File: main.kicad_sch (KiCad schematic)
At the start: 80 parts, among them SW1 Kailh-Choc, SW10 Kailh-Choc, SW11 Kailh-Choc, SW12 Kailh-Choc, SW13 Kailh-Choc, SW14 Kailh-Choc, SW15 Kailh-Choc, SW16 Kailh-Choc, SW17 Kailh-Choc, SW18 Kailh-Choc, SW19 Kailh-Choc, SW2 Kailh-Choc, SW20 Kailh-Choc, SW21 Kailh-Choc, SW22 Kailh-Choc, SW23 Kailh-Choc, SW24 Kailh-Choc, SW25 Kailh-Choc, SW26 Kailh-Choc, SW27 Kailh-Choc, SW28 Kailh-Choc, SW29 Kailh-Choc, SW3 Kailh-Choc, SW30 Kailh-Choc, SW31 Kailh-Choc, SW32 Kailh-Choc, SW33 Kailh-Choc, SW34 Kailh-Choc, SW4 Kailh-Choc, SW5 Kailh-Choc, SW6 Kailh-Choc, SW7 Kailh-Choc, SW8 Kailh-Choc, SW9 Kailh-Choc, U1 nice_nano, U2 nice_nano

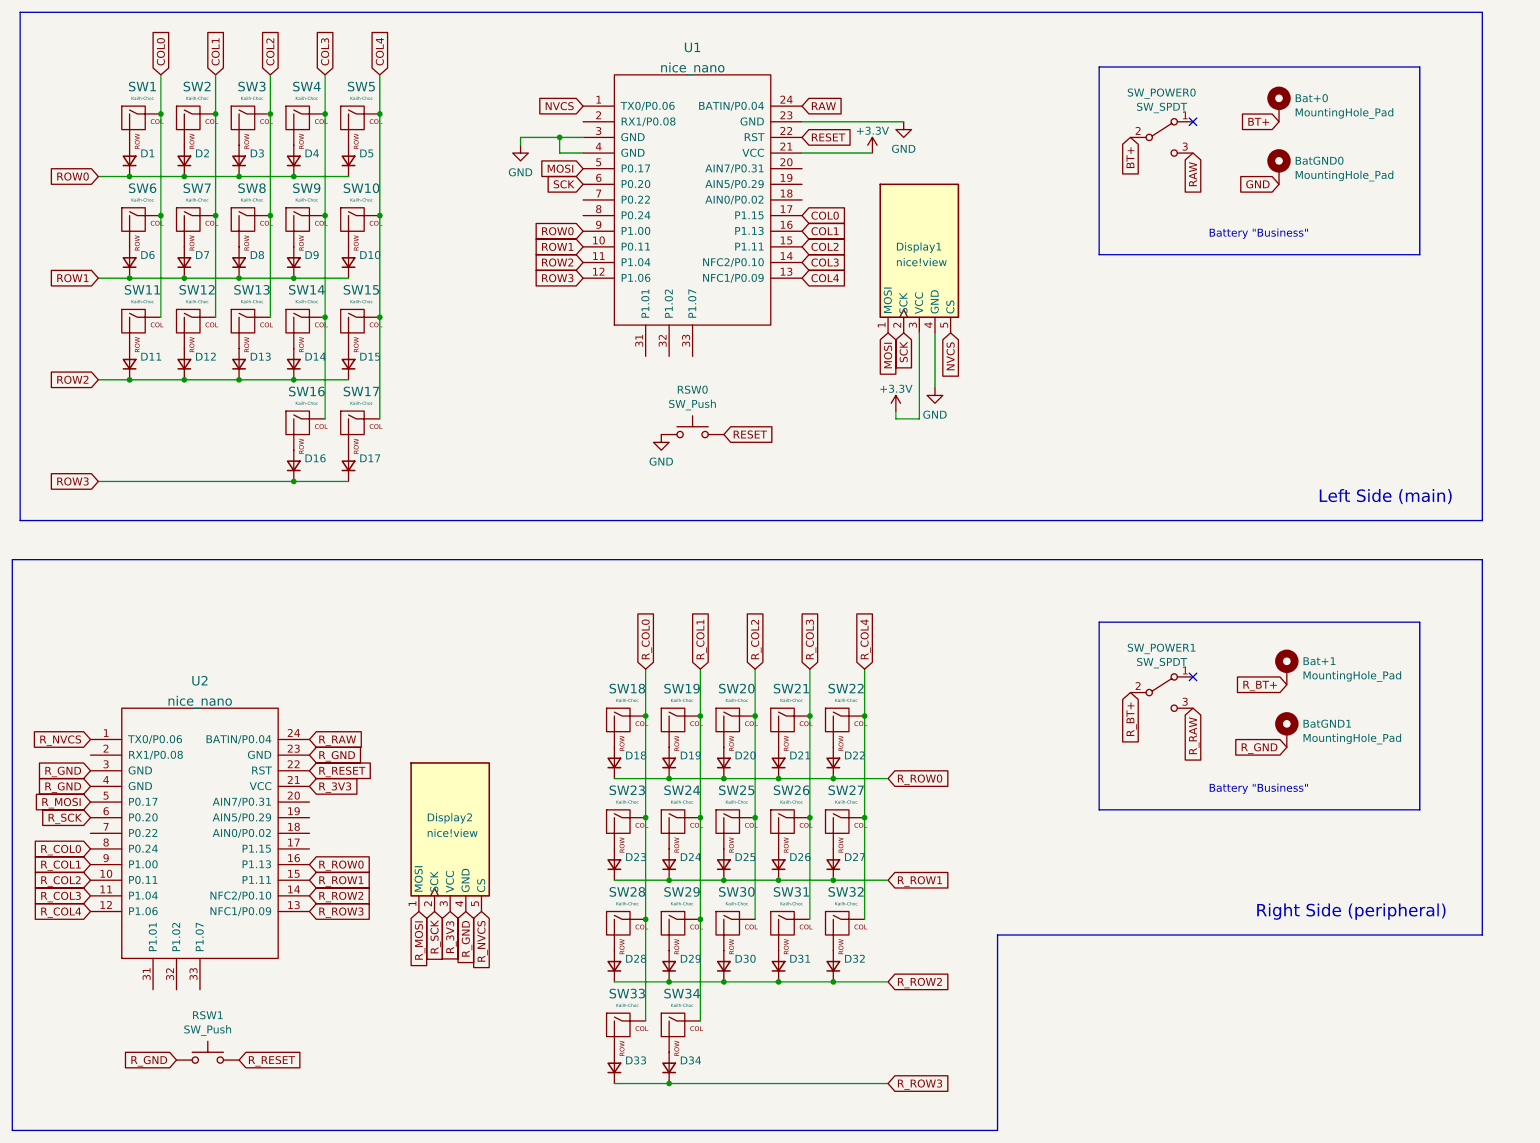
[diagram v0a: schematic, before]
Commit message: Added missing parts to schematic.
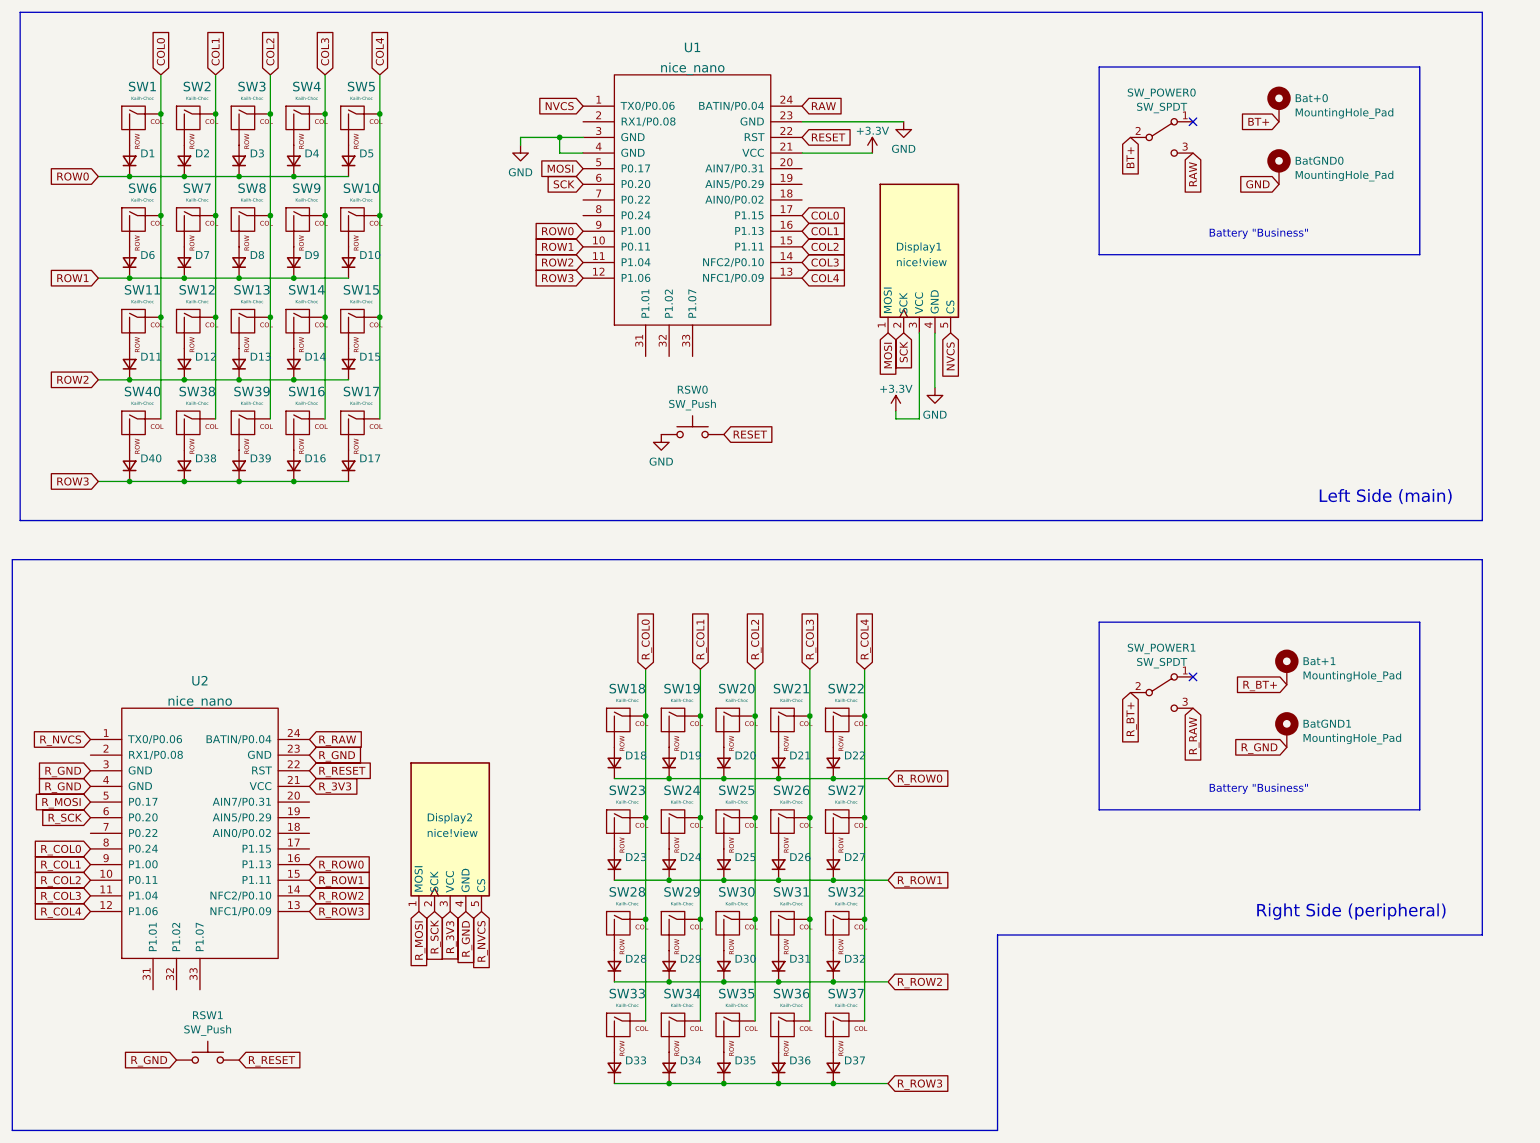
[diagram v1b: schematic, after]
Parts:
- added D35, D36, D37, D38, D39, D40: diode, urchin-footprints:SMD_Diode_Tiny, symbol Device:D_Small
- added SW35, SW36, SW37, SW38, SW39, SW40: Kailh-Choc, urchin-footprints:SW_Hotswap_Kailh_Choc_V1_tweaked, symbol MX_Alps_Hybrid:MX-NoLED
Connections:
- net COL0: now also SW40.1 (COL)
- net COL1: now also SW38.1 (COL)
- net COL2: now also SW39.1 (COL)
- net ROW3: now also D38.1 (K), D39.1 (K), D40.1 (K)
- net R_COL2: now also SW35.1 (COL)
- net R_COL3: now also SW36.1 (COL)
- net R_COL4: now also SW37.1 (COL)
- net R_ROW3: now also D35.1 (K), D36.1 (K), D37.1 (K)
- new net: D35.2 (A), SW35.2 (ROW)
- new net: D37.2 (A), SW37.2 (ROW)
- new net: D36.2 (A), SW36.2 (ROW)
- new net: D39.2 (A), SW39.2 (ROW)
- new net: D40.2 (A), SW40.2 (ROW)
- new net: D38.2 (A), SW38.2 (ROW)

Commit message: Updated schematic and updated pcb
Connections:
- net COL0: now also SW38.1 (COL); no longer SW40.1 (COL)
- net COL1: now also SW39.1 (COL); no longer SW38.1 (COL)
- net COL2: now also SW40.1 (COL); no longer SW39.1 (COL)

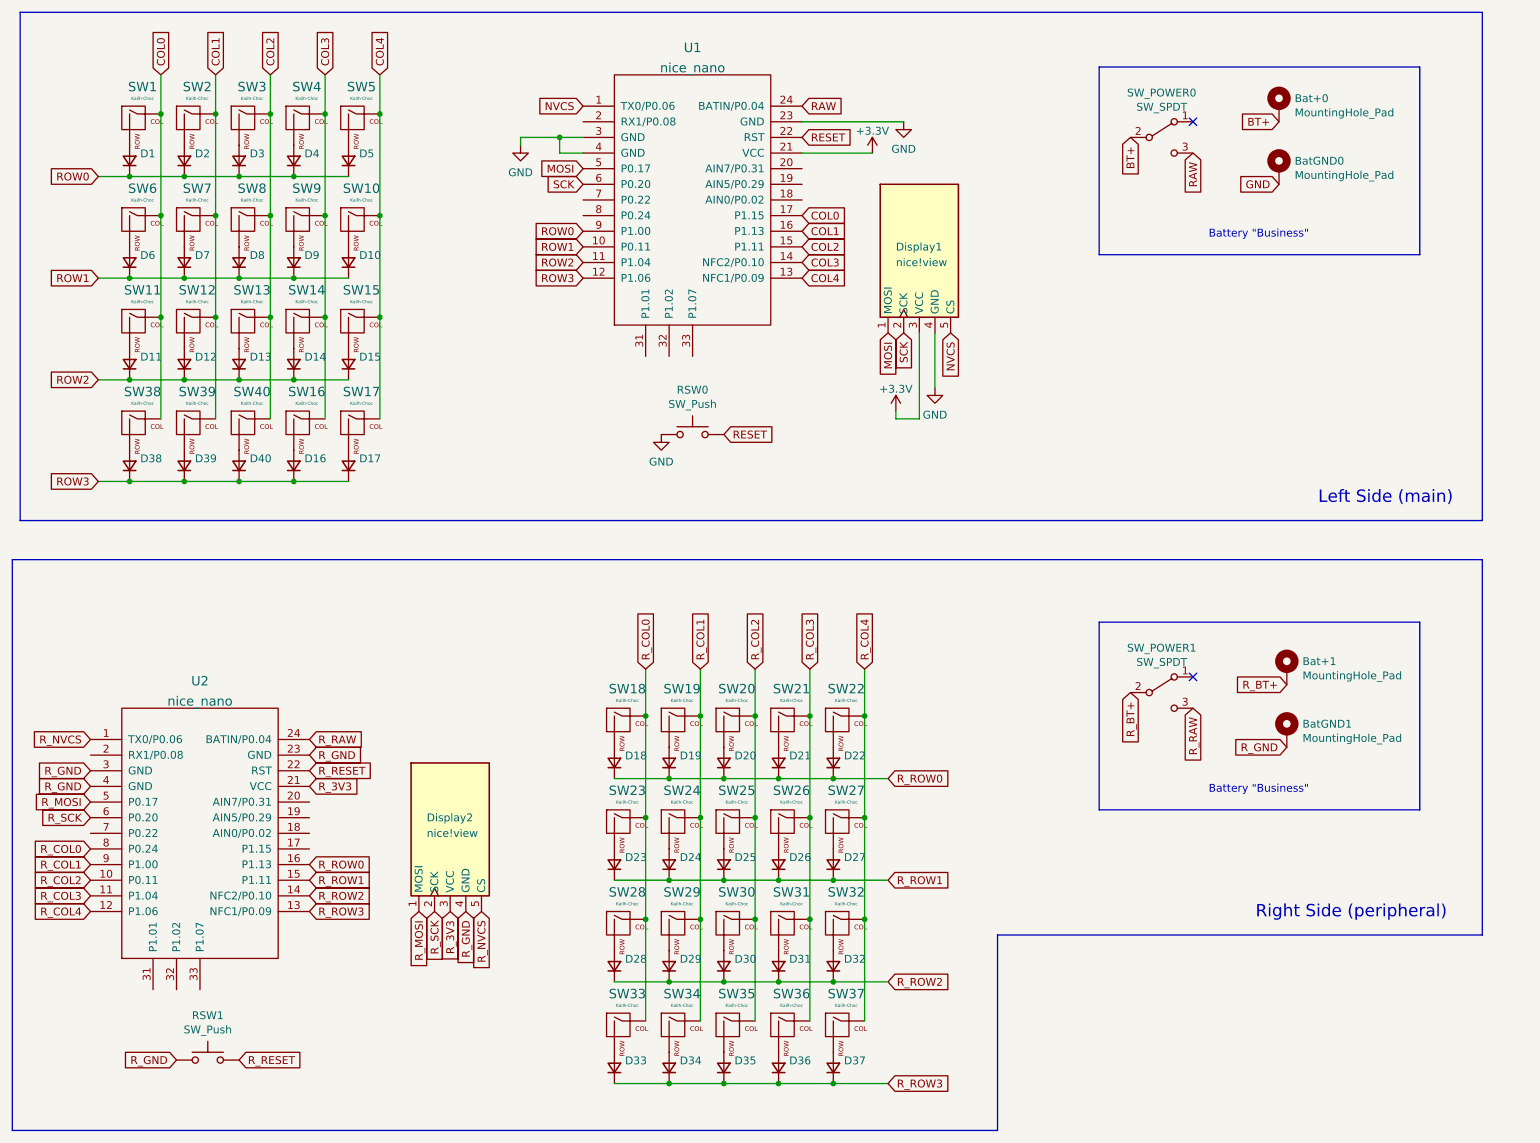
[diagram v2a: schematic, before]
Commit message: Re-annotated all labels
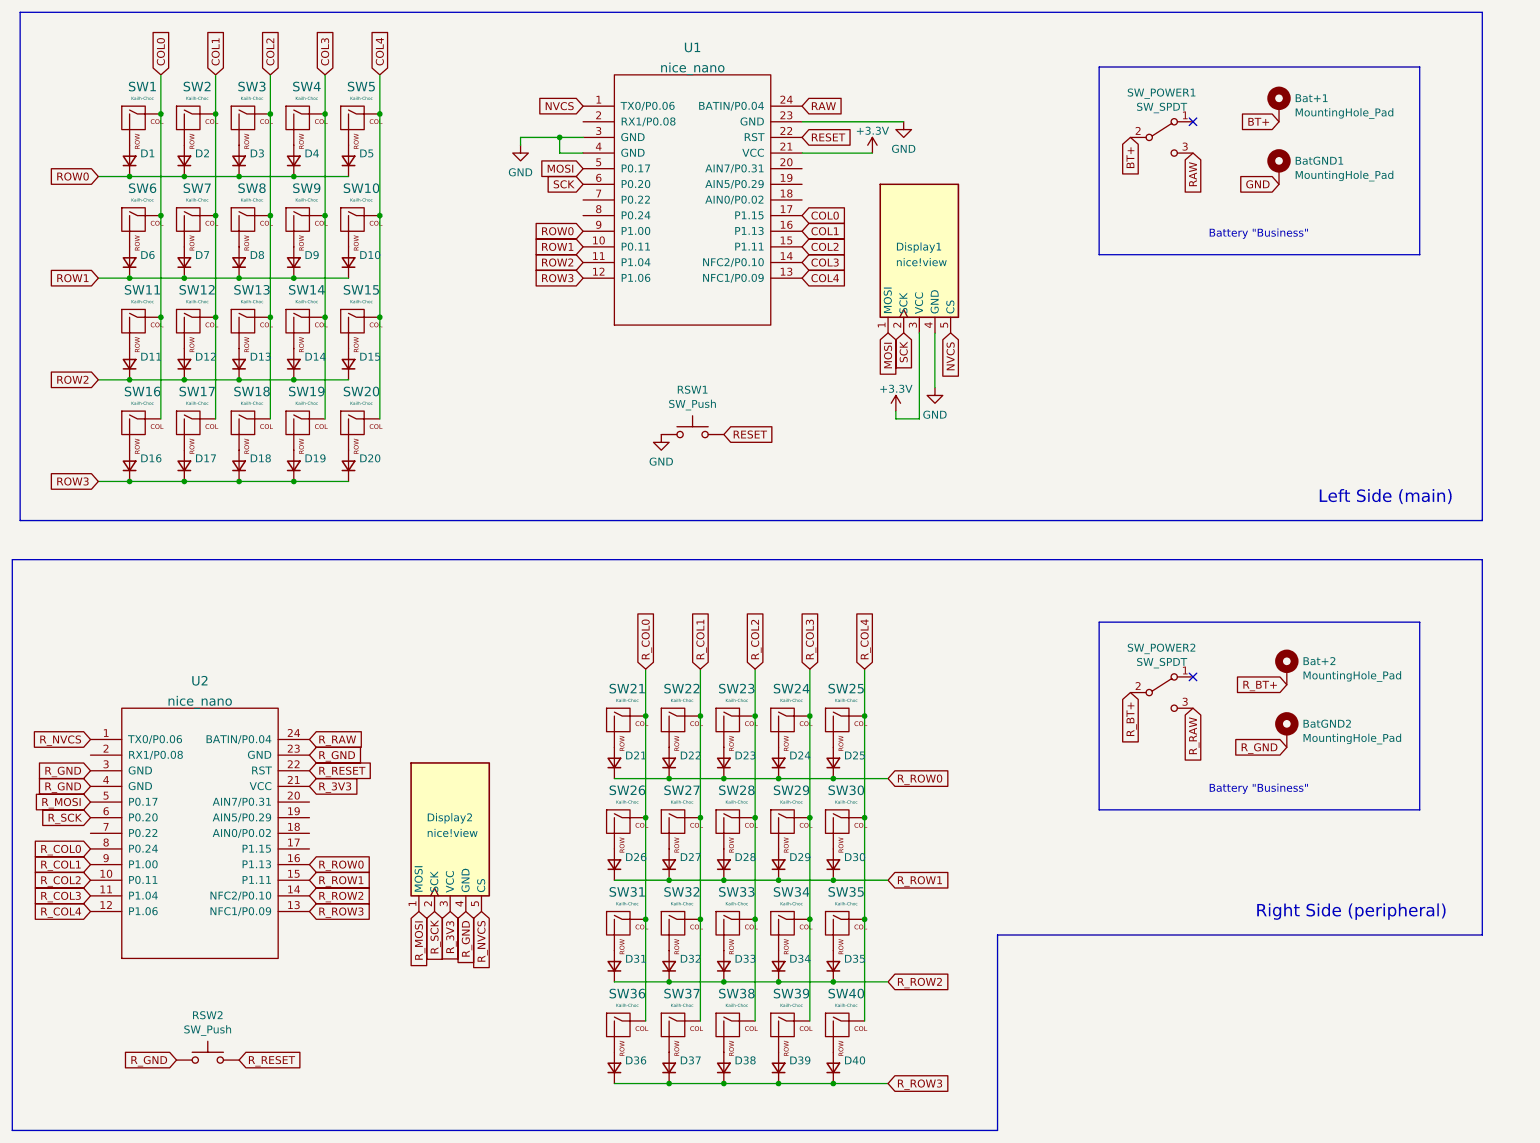
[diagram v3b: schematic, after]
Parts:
- renumbered Bat+0 to Bat+1, Bat+1 to Bat+2, BatGND0 to BatGND1, BatGND1 to BatGND2, D38 to D16, D39 to D17, D40 to D18, D16 to D19, D17 to D20, D18 to D21, D19 to D22, D20 to D23, D21 to D24, D22 to D25, D23 to D26, D24 to D27, D25 to D28, D26 to D29, D27 to D30, D28 to D31, D29 to D32, D30 to D33, D31 to D34, D32 to D35, D33 to D36, D34 to D37, D35 to D38, D36 to D39, D37 to D40, RSW0 to RSW1, RSW1 to RSW2, SW38 to SW16, SW39 to SW17, SW40 to SW18, SW16 to SW19, SW17 to SW20, SW18 to SW21, SW19 to SW22, SW20 to SW23, SW21 to SW24, SW22 to SW25, SW23 to SW26, SW24 to SW27, SW25 to SW28, SW26 to SW29, SW27 to SW30, SW28 to SW31, SW29 to SW32, SW30 to SW33, SW31 to SW34, SW32 to SW35, SW33 to SW36, SW34 to SW37, SW35 to SW38, SW36 to SW39, SW37 to SW40, SW_POWER0 to SW_POWER1, SW_POWER1 to SW_POWER2
